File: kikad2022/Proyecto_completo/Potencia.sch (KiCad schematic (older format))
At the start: 73 parts, among them J11 Conn_01x01_Male, J16 Conn_01x01_Male, J17 Conn_01x02_Male, J18 Conn_01x01_Male, J19 Conn_01x01_Male, J20 V_Triang_RF, J21 Conn_01x01_Male, Q17 BC557, Q18 BC547, Q19 IRF510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

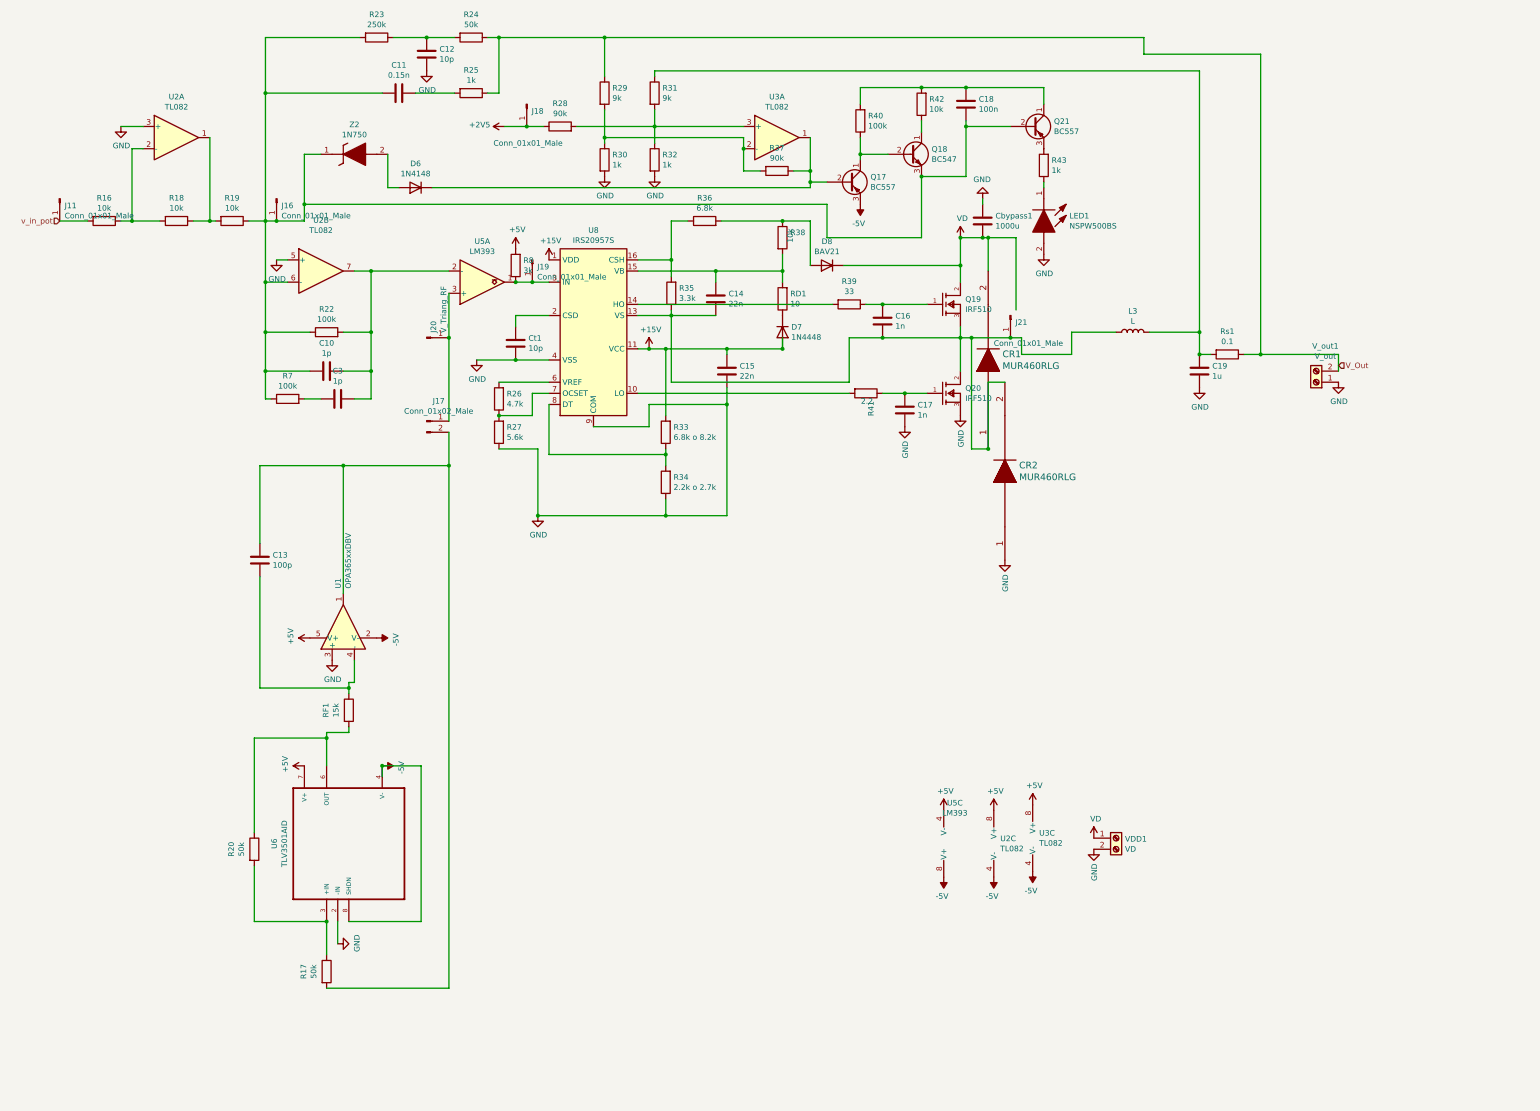
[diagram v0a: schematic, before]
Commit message: kikad_modificaciones
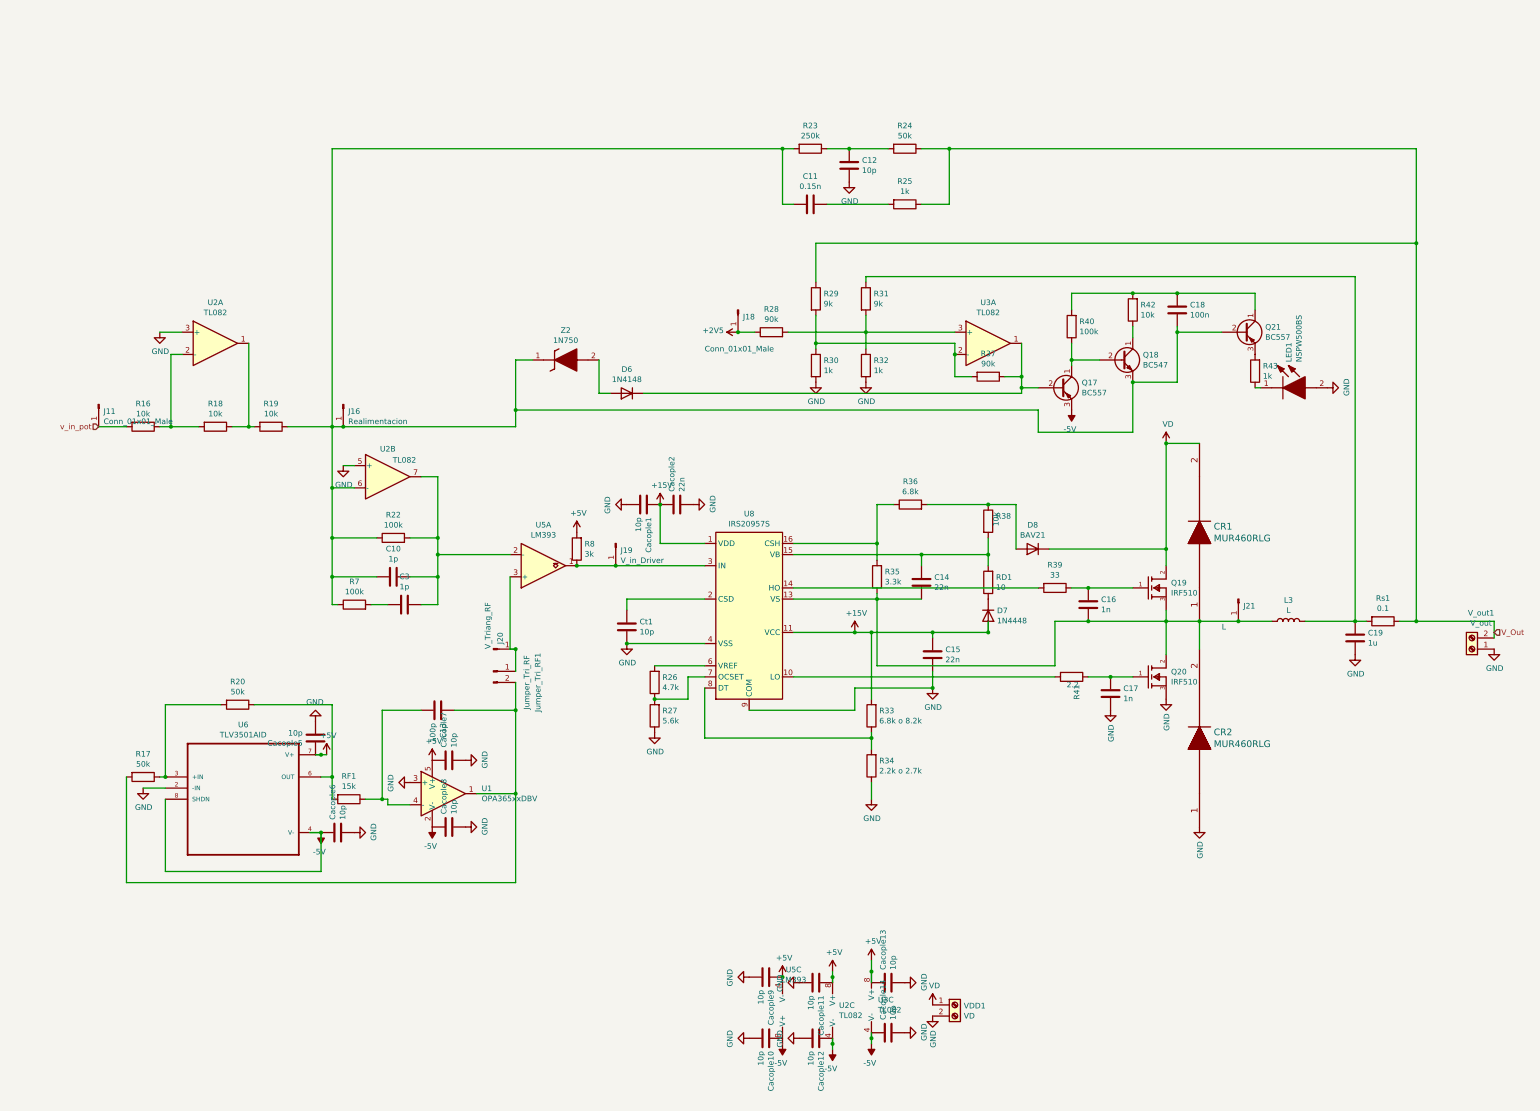
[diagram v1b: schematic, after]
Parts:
- removed Cbypass1: 1000u, Capacitor_THT:C_Radial_D16.0mm_H25.0mm_P7.50mm, symbol Device:C
- added Cacople1, Cacople10, Cacople11, Cacople12, Cacople13, Cacople14, Cacople5, Cacople6, Cacople7, Cacople8, Cacople9: 10p, Capacitor_SMD:C_0603_1608Metric, symbol Device:C
- added Cacople2: 22n, New folder:CAPPRD500W65D1000H1350, symbol Device:C
- J16: value Conn_01x01_Male -> Realimentacion
- J19: value Conn_01x01_Male -> V_in_Driver
- J21: value Conn_01x01_Male -> L
- Jumper_Tri_RF1: renamed from J17; value Conn_01x02_Male -> Jumper_Tri_RF
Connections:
- net +15V: now also Cacople1.2, Cacople2.2
- net +5V: now also Cacople11.2, Cacople13.2, Cacople5.2, Cacople7.2, Cacople9.2
- net -5V: now also Cacople12.2, Cacople14.2, Cacople6.2, Cacople8.2
- net GND: now also Cacople1.1, Cacople10.1, Cacople11.1, Cacople12.1, Cacople13.1, Cacople14.1, Cacople2.1, Cacople5.1, Cacople6.1, Cacople7.1, Cacople8.1, Cacople9.1
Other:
- moved on the sheet: C10, C11, C12, C13, C14, C15, C16, C17, C18, C19, C3, CR1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
